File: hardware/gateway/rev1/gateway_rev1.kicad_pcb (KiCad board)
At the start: 2 copper layers, 100 x 45 mm, 80 parts, among them IC1 STM8L151K4T6, IC2 CC1101RGPR, IC3 LT1615ES5-1#TRMPBF, IC4 MIC4427YM, IC5 MB85RC64TAPNF-G-BDERE1, J1 G8250041000YEU, J2 M20-9770342, Q1 IRLML6402TRPBF, U1 2462, Y1 NX3225GA-26.000M-STD-CRG-2

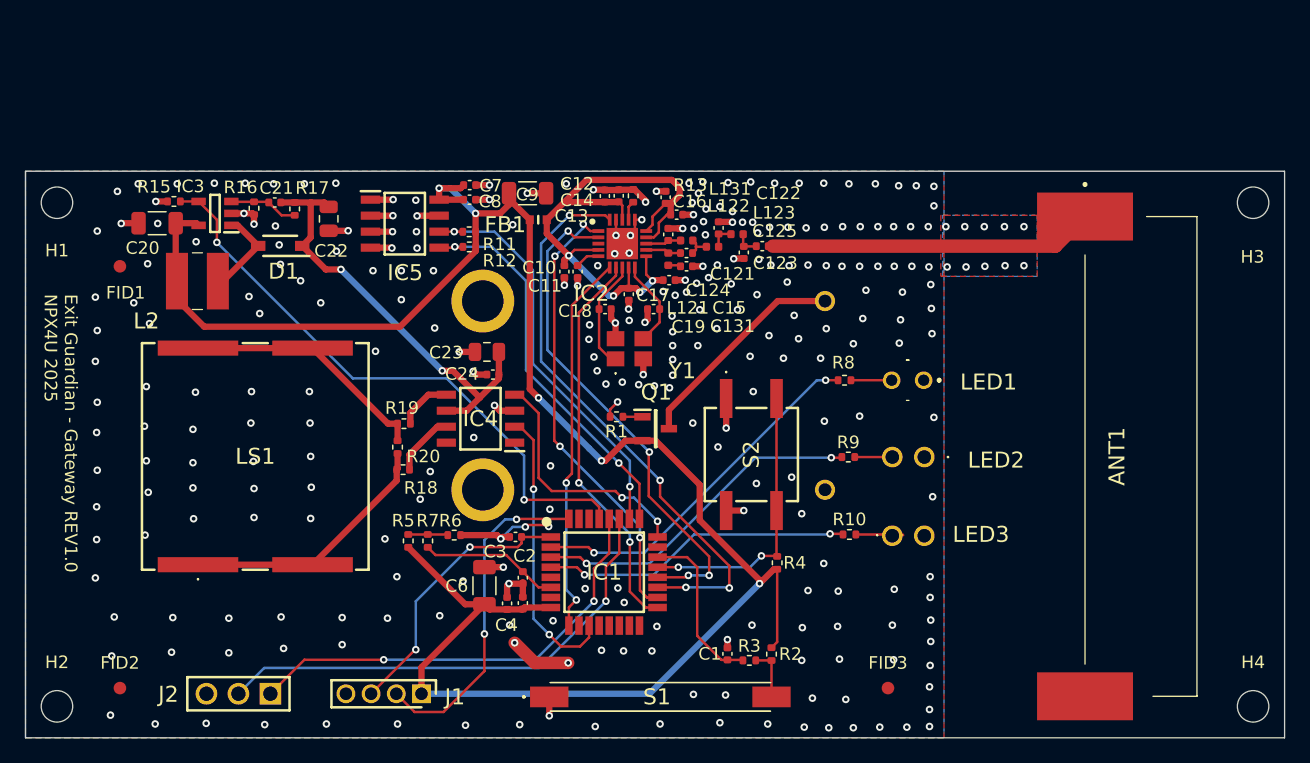
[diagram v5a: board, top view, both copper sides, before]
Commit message: Replaced 0402  by 0603 package where was possible.
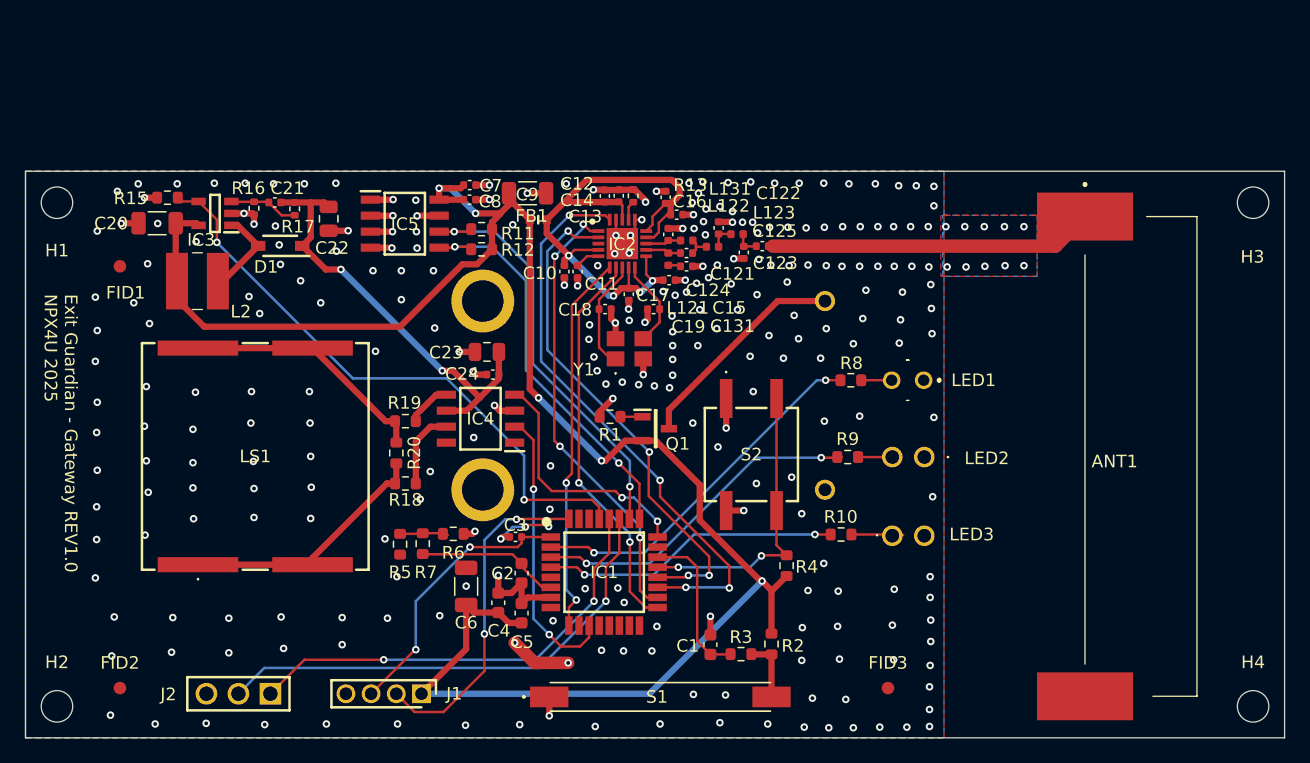
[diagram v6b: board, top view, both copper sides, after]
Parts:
- C1, C2, C4, C5: footprint Capacitor_SMD:C_0402_1005Metric -> Capacitor_SMD:C_0603_1608Metric
- R1, R11, R12, R15, R18, R19, R2, R20, R3, R4, R5, R6, R7, R8: footprint Resistor_SMD:R_0402_1005Metric -> Resistor_SMD:R_0603_1608Metric
- R10, R9: value 50 -> 47; footprint Resistor_SMD:R_0402_1005Metric -> Resistor_SMD:R_0603_1608Metric
- moved C1 1.53 mm to (233.9, 152.6)
- moved C6 1.45 mm to (214.5, 147.9)
- moved R18 1.12 mm to (209.7, 139.8)
- moved R11 1.01 mm to (215.7, 119.5)
- moved R12 0.99 mm to (215.7, 121.2)
- moved R3 0.83 mm to (236.3, 153.3)
- moved C5 0.81 mm to (218.9, 150.1)
- moved R2 0.80 mm to (238.8, 152.5)
- moved R4 0.78 mm to (239.9, 146.3)
- moved R5 0.70 mm to (209.2, 144.6)
- moved C4 0.70 mm to (217.1, 149.2)
- moved R10 0.66 mm to (244.3, 143.8)
- moved R15 0.60 mm to (190.8, 117.0)
- moved R1 0.51 mm to (225.9, 134.4)
- moved R8 0.50 mm to (245.1, 131.6)
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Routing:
- net VDD: track 157.0 -> 147.4 mm
- net GND: track 75.7 -> 77.1 mm, vias 289 -> 287
- net Net-(IC4-OUTA): track 5.04 -> 6.25 mm
- net LED_R: track 24.8 -> 23.8 mm
- net BTN: track 22.5 -> 23.4 mm
- net DOOR: track 13.4 -> 12.5 mm
- net Net-(R2-Pad1): track 4.14 -> 4.99 mm
- net Net-(LED1-A): track 3.24 -> 2.42 mm
- net SCL: track 32.8 -> 33.5 mm
- net Net-(IC4-OUTB): track 4.32 -> 3.57 mm
- net SDA: track 31.4 -> 32.1 mm

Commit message: DRC errors fixed and silkscreen fixed.
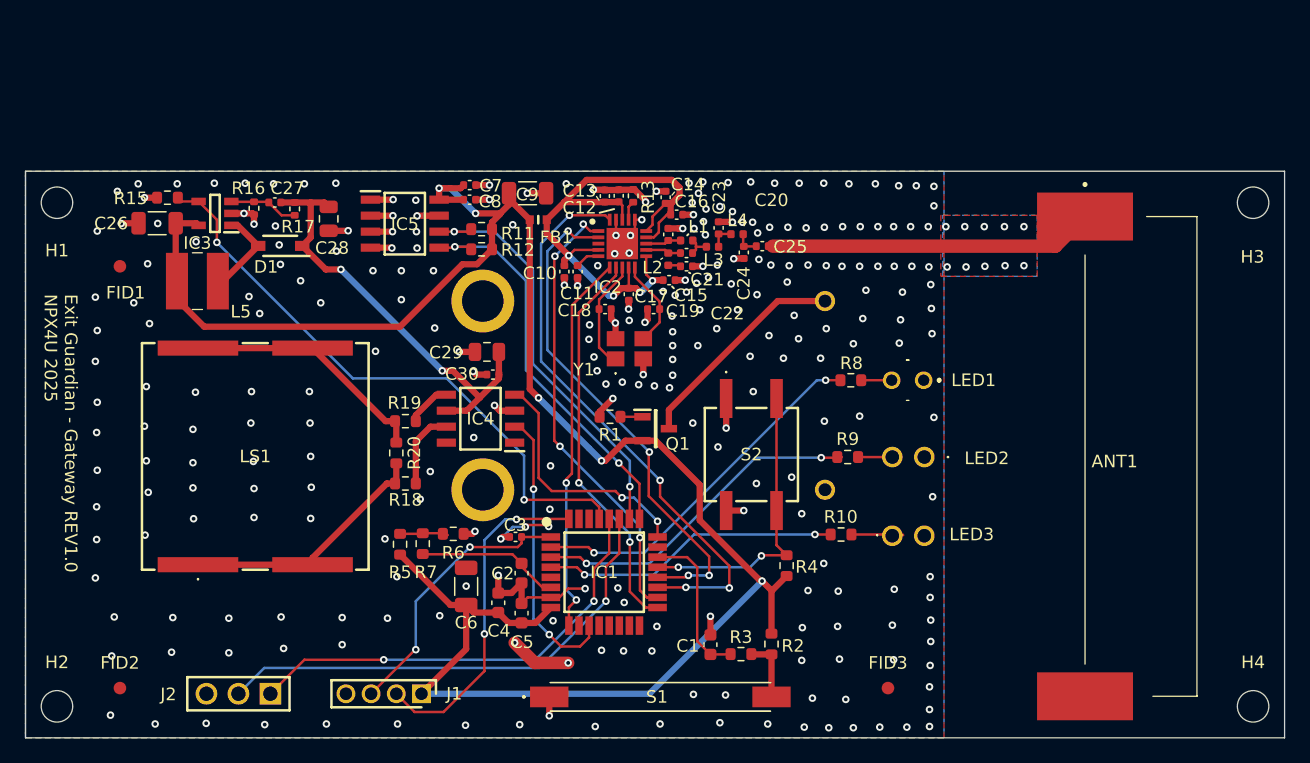
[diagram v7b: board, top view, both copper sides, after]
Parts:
- renumbered C131 to C20, C124 to C21, C121 to C22, C122 to C23, C123 to C24, C125 to C25, C20 to C26, C21 to C27, C22 to C28, C23 to C29, C24 to C30, L131 to L1, L121 to L2, L122 to L3, L123 to L4, L2 to L5
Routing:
- net VDD: track 147.4 -> 157.1 mm
- net GND: track 77.1 -> 80.1 mm
